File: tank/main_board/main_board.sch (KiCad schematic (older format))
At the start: 38 parts, among them J1 PowerIn, J10 Bump1, J11 Programming Header, J12 SigOut, J13 Encoder0, J14 Encoder1, J16 PowerOut, J2 M1, J20 PowerMotor, J3 M2, J4 LEDs, J5 M0, J6 Spk, J7 Hall2, J8 Hall1, J9 Bump0, Q1 2N3904, U1 L7805, U2 ATMEGA328P-PU, U3 SN74HC595, U4 TB6612FNG, U5 TB6612FNG, Y1 Crystal

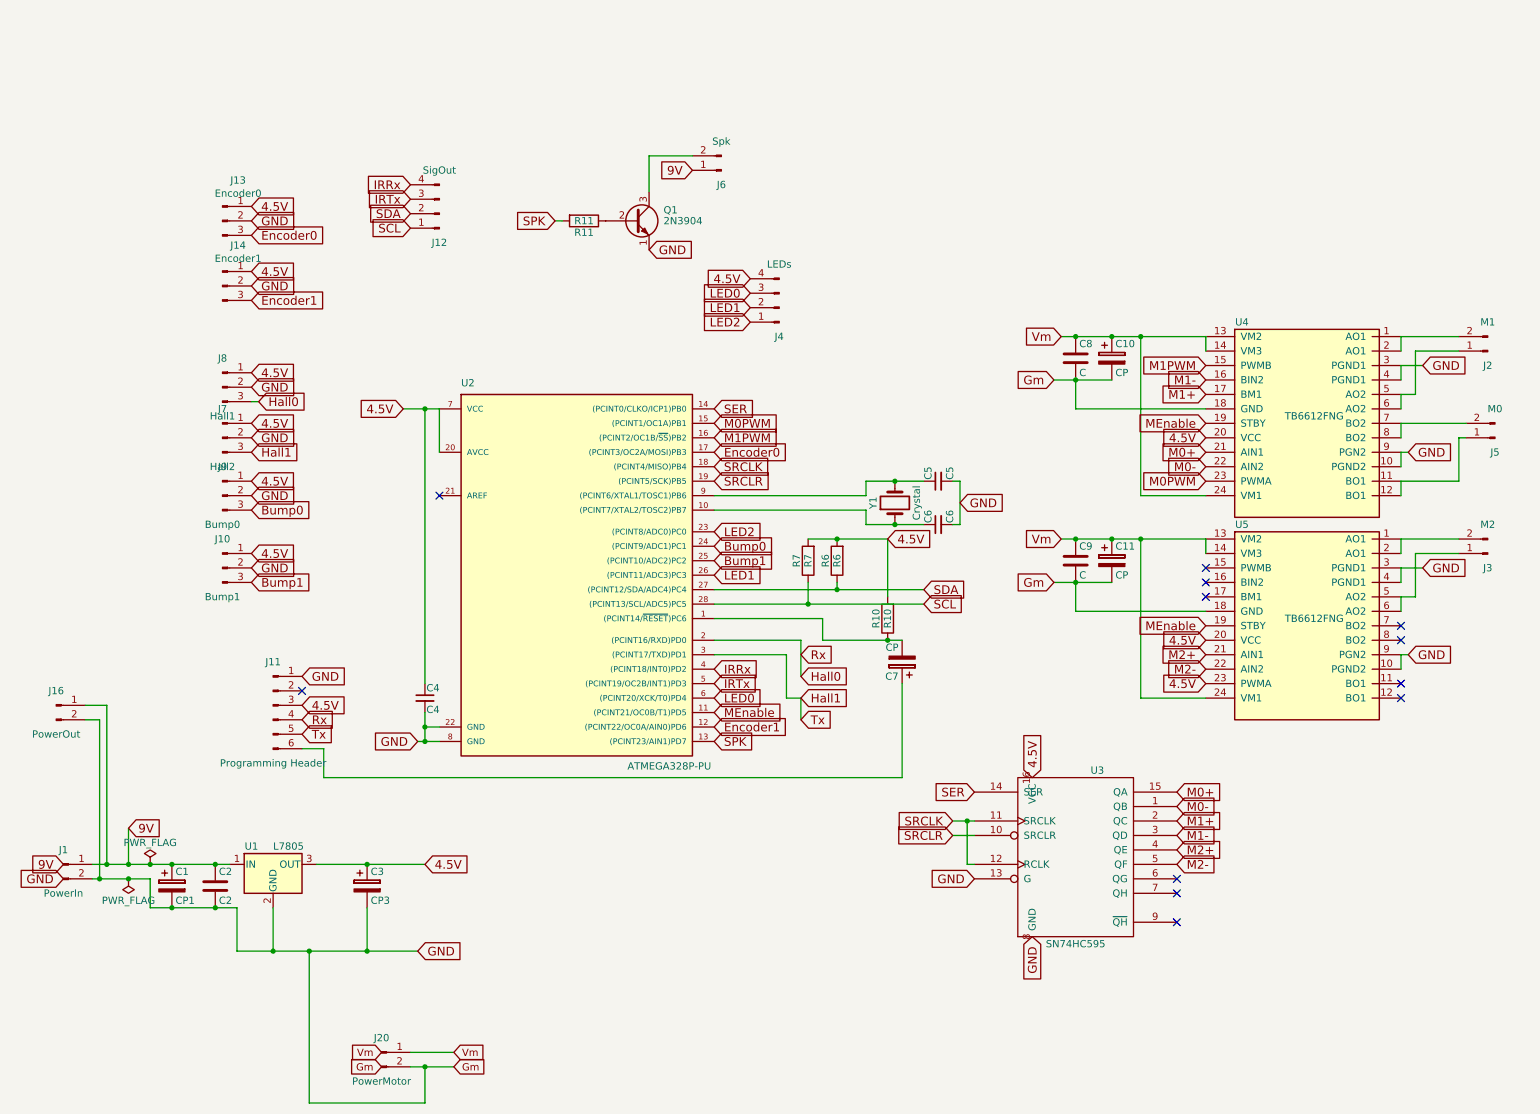
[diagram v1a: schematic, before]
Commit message: Main Board version 0.6: - add ground planes on both layers - LED square is VCC - shorten board slightly - power out is regulated - vias. vias everywhere. - mounting holes embiggened
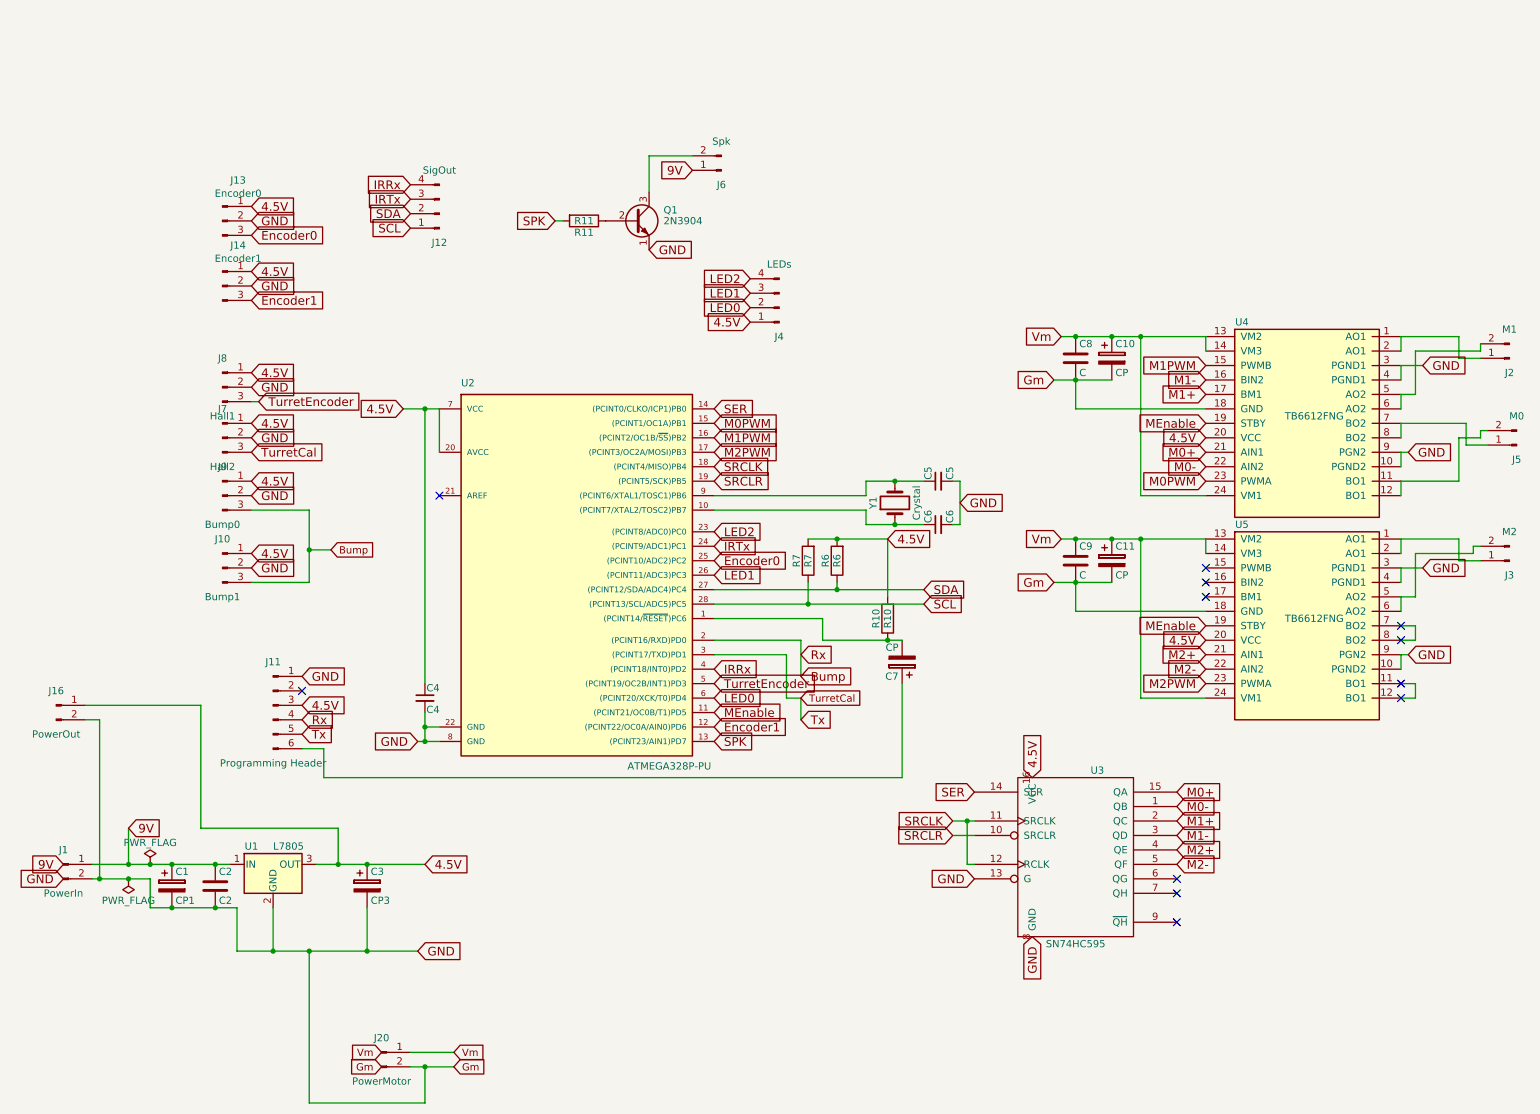
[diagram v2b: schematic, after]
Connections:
- net 4.5V: now also J16.1 (Pin_1), J4.1 (Pin_1); no longer J4.4 (Pin_4), U5.23 (PWMA)
- net 9V: no longer J16.1 (Pin_1)
- net Encoder0: now also U2.25 ((PCINT10/ADC2)PC2); no longer U2.17 ((PCINT3/OC2A/MOSI)PB3)
- net IRTx: now also U2.24 ((PCINT9/ADC1)PC1); no longer U2.5 ((PCINT19/OC2B/INT1)PD3)
- net LED0: now also J4.2 (Pin_2); no longer J4.3 (Pin_3)
- net LED1: now also J4.3 (Pin_3); no longer J4.2 (Pin_2)
- net LED2: now also J4.4 (Pin_4); no longer J4.1 (Pin_1)
- net at U4.1 (AO1), U4.2 (AO1): now also J2.1 (Pin_1); no longer J2.2 (Pin_2)
- net at U4.11 (BO1), U4.12 (BO1): now also J5.2 (Pin_2); no longer J5.1 (Pin_1)
- net at U4.5 (AO2), U4.6 (AO2): now also J2.2 (Pin_2); no longer J2.1 (Pin_1)
- net at U4.7 (BO2), U4.8 (BO2): now also J5.1 (Pin_1); no longer J5.2 (Pin_2)
- net at U5.1 (AO1), U5.2 (AO1): now also J3.1 (Pin_1); no longer J3.2 (Pin_2)
- net at U5.11 (BO1): now also U5.12 (BO1)
- net at U5.5 (AO2), U5.6 (AO2): now also J3.2 (Pin_2); no longer J3.1 (Pin_1)
- net at U5.7 (BO2): now also U5.8 (BO2)
- net Bump0 renamed Bump
- net Bump: now also J10.3 (Pin_3), J11.4 (Pin_4), U2.2 ((PCINT16/RXD)PD0); no longer U2.24 ((PCINT9/ADC1)PC1)
- removed net Bump1: J10.3 (Pin_3), U2.25 ((PCINT10/ADC2)PC2)
- removed net Hall0: J11.4 (Pin_4), J8.3 (Pin_3), U2.2 ((PCINT16/RXD)PD0)
- net Hall1 renamed TurretCal
- new net M2PWM: U2.17 ((PCINT3/OC2A/MOSI)PB3), U5.23 (PWMA)
- new net TurretEncoder: J8.3 (Pin_3), U2.5 ((PCINT19/OC2B/INT1)PD3)
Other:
- moved on the sheet: J2, J3, J5
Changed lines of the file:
@@
-$EndComp
-$Comp
-L main_board-rescue:Conn_01x03_Male J9
-U 1 1 59DE306D
-P 1850 3000
-F 0 "J9" H 1850 3200 50  0000 C CNN
-F 1 "Bump0" H 1850 2800 50  0000 C CNN
-F 2 "JST:JST_EH_B03B-EH-A_03x2.50mm_Straight" H 1850 3000 50  0001 C CNN
-F 3 "" H 1850 3000 50  0001 C CNN
-	1    1850 3000
-	1    0    0    -1
 $EndComp
 $Comp
@@
 $EndComp
 Wire Wire Line
-	950  5550 1050 5550
-Wire Wire Line
 	950  5650 1000 5650
 Wire Wire Line
@@
 Wire Wire Line
 	1200 5550 1200 5300
-Wire Wire Line
-	1050 4450 1050 5550
-Wire Wire Line
-	1050 4450 900  4450
-Connection ~ 1050 5550
 Wire Wire Line
 	900  4550 1000 4550
@@
 Text GLabel 5250 4200 2    60   Input ~ 0
 IRRx
-Text GLabel 5250 4300 2    60   Input ~ 0
+Text GLabel 5250 3350 2    60   Input ~ 0
 IRTx
 Text GLabel 6950 3050 2    60   Input ~ 0
@@
 	10100 2300 10100 2000
 Wire Wire Line
-	10100 2000 10400 2000
-Wire Wire Line
 	10000 2400 10000 2300
 Wire Wire Line
@@
 Wire Wire Line
 	10400 2900 10400 2600
-Wire Wire Line
-	10400 2600 10450 2600
 NoConn ~ 8450 5650
 NoConn ~ 8450 5750
@@
 Text GLabel 7600 2200 0    60   Input ~ 0
 Gm
+Wire Wire Line
+	5250 4000 5850 4000
+Wire Wire Line
+	5850 4000 5850 4250
+Wire Wire Line
+	5250 4100 5750 4100
+Wire Wire Line
+	5750 4100 5750 4400
+Wire Wire Line
+	5750 4400 5850 4400
 Text GLabel 5850 4250 2    60   Input ~ 0
-Hall0
-Text GLabel 5850 4400 2    60   Input ~ 0
-Hall1
-Wire Wire Line
-	5250 4000 5850 4000
-Wire Wire Line
-	5850 4000 5850 4250
-Wire Wire Line
-	5250 4100 5750 4100
-Wire Wire Line
-	5750 4100 5750 4400
-Wire Wire Line
-	5750 4400 5850 4400
-Text GLabel 5250 3450 2    60   Input ~ 0
-Bump1
-Text GLabel 2050 3600 2    60   Input ~ 0
-Bump1
-Text GLabel 5250 3350 2    60   Input ~ 0
-Bump0
-Text GLabel 2050 3100 2    60   Input ~ 0
-Bump0
+Bump
 Text GLabel 2100 2350 2    60   Input ~ 0
-Hall0
+TurretEncoder
 Text GLabel 2050 2700 2    60   Input ~ 0
-Hall1
+TurretCal
+Text GLabel 5500 1800 0    60   Input ~ 0
+4.5V
+Text GLabel 5500 1700 0    60   Input ~ 0
+LED0
+Text GLabel 5500 1600 0    60   Input ~ 0
+LED1
 Text GLabel 5500 1500 0    60   Input ~ 0
-4.5V
-Text GLabel 5500 1600 0    60   Input ~ 0
-LED0
-Text GLabel 5500 1700 0    60   Input ~ 0
-LED1
-Text GLabel 5500 1800 0    60   Input ~ 0
 LED2
 Text GLabel 5250 2500 2    60   Input ~ 0
@@
 Text GLabel 8650 2100 0    60   Input ~ 0
 M1PWM
-Text GLabel 5250 2700 2    60   Input ~ 0
+Text GLabel 5250 3450 2    60   Input ~ 0
 Encoder0
 Text GLabel 5250 2400 2    60   Input ~ 0
@@
 Wire Wire Line
 	10100 3700 10100 3400
-Wire Wire Line
-	10100 3400 10400 3400
 Text GLabel 7650 3300 0    60   Input ~ 0
 Vm
@@
 	6100 3650 6700 3650
 Wire Wire Line
-	1050 5550 1200 5550
-Wire Wire Line
 	6450 4000 6550 4000
 Wire Wire Line
@@
 	6950 2900 6950 3200
 Wire Wire Line
-	2500 5550 2850 5550
+	2500 5550 2650 5550
 Wire Wire Line
 	1000 5650 1200 5650
@@
 Wire Wire Line
 	7750 3800 7750 3600
-Text GLabel 8650 4300 0    60   Input ~ 0
-4.5V
 $Comp
 L main_board-rescue:Conn_01x03_Male J13
@@
 L main_board-rescue:Conn_01x02_Male J2
 U 1 1 5E9835C0
-P 10600 2000
-F 0 "J2" H 10600 2100 50  0000 C CNN
-F 1 "M1" H 10600 1800 50  0000 C CNN
-F 2 "JST:JST_EH_B02B-EH-A_02x2.50mm_Straight" H 10600 2000 50  0001 C CNN
-F 3 "" H 10600 2000 50  0001 C CNN
-	1    10600 2000
+P 10750 2050
+F 0 "J2" H 10750 2150 50  0000 C CNN
+F 1 "M1" H 10750 1850 50  0000 C CNN
+F 2 "JST:JST_EH_B02B-EH-A_02x2.50mm_Straight" H 10750 2050 50  0001 C CNN
+F 3 "" H 10750 2050 50  0001 C CNN
+	1    10750 2050
 	-1   0    0    1
 $EndComp
@@
 L main_board-rescue:Conn_01x02_Male J5
 U 1 1 5E98A5F8
-P 10650 2600
-F 0 "J5" H 10650 2700 50  0000 C CNN
-F 1 "M0" H 10650 2400 50  0000 C CNN
-F 2 "JST:JST_EH_B02B-EH-A_02x2.50mm_Straight" H 10650 2600 50  0001 C CNN
-F 3 "" H 10650 2600 50  0001 C CNN
-	1    10650 2600
+P 10800 2650
+F 0 "J5" H 10800 2750 50  0000 C CNN
+F 1 "M0" H 10800 2450 50  0000 C CNN
+F 2 "JST:JST_EH_B02B-EH-A_02x2.50mm_Straight" H 10800 2650 50  0001 C CNN
+F 3 "" H 10800 2650 50  0001 C CNN
+	1    10800 2650
 	-1   0    0    1
 $EndComp
+Text GLabel 5250 2700 2    60   Input ~ 0
+M2PWM
+Text GLabel 8650 4300 0    60   Input ~ 0
+M2PWM
+Text GLabel 5250 4300 2    60   Input ~ 0
+TurretEncoder
+$Comp
+L main_board-rescue:Conn_01x03_Male J9
+U 1 1 59DE306D
+P 1850 3000
+F 0 "J9" H 1850 3200 50  0000 C CNN
+F 1 "Bump0" H 1850 2800 50  0000 C CNN
+F 2 "JST:JST_EH_B03B-EH-A_03x2.50mm_Straight" H 1850 3000 50  0001 C CNN
+F 3 "" H 1850 3000 50  0001 C CNN
+	1    1850 3000
+	1    0    0    -1
+$EndComp
+Wire Wire Line
+	2050 3100 2450 3100
+Wire Wire Line
+	2450 3100 2450 3375
+Wire Wire Line
+	2450 3375 2600 3375
+Wire Wire Line
+	2450 3600 2450 3375
+Connection ~ 2450 3375
+Text GLabel 2600 3375 2    50   Input ~ 0
+Bump
+Wire Wire Line
+	2450 3600 2050 3600
+Text GLabel 5850 4400 2    50   Input ~ 0
+TurretCal
 $Comp
 L main_board-rescue:Conn_01x02_Male J3
 U 1 1 5E98F9A1
-P 10600 3400
-F 0 "J3" H 10600 3500 50  0000 C CNN
-F 1 "M2" H 10600 3200 50  0000 C CNN
-F 2 "JST:JST_EH_B02B-EH-A_02x2.50mm_Straight" H 10600 3400 50  0001 C CNN
-F 3 "" H 10600 3400 50  0001 C CNN
-	1    10600 3400
+P 10750 3450
+F 0 "J3" H 10750 3550 50  0000 C CNN
+F 1 "M2" H 10750 3250 50  0000 C CNN
+F 2 "JST:JST_EH_B02B-EH-A_02x2.50mm_Straight" H 10750 3450 50  0001 C CNN
+F 3 "" H 10750 3450 50  0001 C CNN
+	1    10750 3450
 	-1   0    0    1
 $EndComp
+Wire Wire Line
+	10550 2000 10550 1950
+Wire Wire Line
+	10100 2000 10550 2000
+Wire Wire Line
+	10400 1900 10400 2050
+Wire Wire Line
+	10400 2050 10550 2050
+Wire Wire Line
+	10550 2600 10550 2550
+Wire Wire Line
+	10550 2550 10600 2550
+Wire Wire Line
+	10400 2600 10550 2600
+Wire Wire Line
+	10450 2500 10450 2650
+Wire Wire Line
+	10450 2650 10600 2650
+Wire Wire Line
+	10500 3400 10500 3350
+Wire Wire Line
+	10500 3350 10550 3350
+Wire Wire Line
+	10100 3400 10500 3400
+Wire Wire Line
+	10400 3300 10400 3450
+Wire Wire Line
+	10400 3450 10550 3450
+Wire Wire Line
+	10000 4000 10100 4000
+Wire Wire Line
+	10100 4000 10100 3900
+Wire Wire Line
+	10100 3900 10000 3900
+Wire Wire Line
+	10000 4300 10100 4300
+Wire Wire Line
+	10100 4300 10100 4400
+Wire Wire Line
+	10100 4400 10000 4400
+Wire Wire Line
+	950  5550 1200 5550
+Wire Wire Line
+	1700 4450 1700 5300
+Wire Wire Line
+	1700 5300 2650 5300
+Wire Wire Line
+	2650 5300 2650 5550
+Wire Wire Line
+	900  4450 1700 4450
+Connection ~ 2650 5550
+Wire Wire Line
+	2650 5550 2850 5550
 $EndSCHEMATC

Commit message: Main Board Version 0.7
Had to switch around pins. Need M0 and M1 on the same PWM timer.
Need IR receiver pin to not interfere.
No point in ground traces with a ground plane.
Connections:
- net Encoder1: now also U2.17 ((PCINT3/OC2A/MOSI)PB3); no longer U2.12 ((PCINT22/OC0A/AIN0)PD6)
- net IRRx: now also U2.5 ((PCINT19/OC2B/INT1)PD3); no longer U2.4 ((PCINT18/INT0)PD2)
- net M0PWM: now also U2.11 ((PCINT21/OC0B/T1)PD5); no longer U2.15 ((PCINT1/OC1A)PB1)
- net M1PWM: now also U2.12 ((PCINT22/OC0A/AIN0)PD6); no longer U2.16 ((PCINT2/OC1B/~SS~)PB2)
- net M2PWM: now also U2.15 ((PCINT1/OC1A)PB1); no longer U2.17 ((PCINT3/OC2A/MOSI)PB3)
- net MEnable: now also U2.16 ((PCINT2/OC1B/~SS~)PB2); no longer U2.11 ((PCINT21/OC0B/T1)PD5)
- net TurretEncoder: now also U2.4 ((PCINT18/INT0)PD2); no longer U2.5 ((PCINT19/OC2B/INT1)PD3)
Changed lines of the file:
@@
 Text GLabel 2050 3500 2    60   Input ~ 0
 GND
-Text GLabel 5250 4500 2    60   Input ~ 0
+Text GLabel 5250 2600 2    60   Input ~ 0
 MEnable
 Text GLabel 5250 4400 2    60   Input ~ 0
@@
 Text GLabel 3100 2400 0    60   Input ~ 0
 4.5V
-Text GLabel 5250 4200 2    60   Input ~ 0
+Text GLabel 5250 4300 2    60   Input ~ 0
 IRRx
 Text GLabel 5250 3350 2    60   Input ~ 0
@@
 Text GLabel 5500 1500 0    60   Input ~ 0
 LED2
-Text GLabel 5250 2500 2    60   Input ~ 0
+Text GLabel 5250 4500 2    60   Input ~ 0
 M0PWM
 Text GLabel 8650 2900 0    60   Input ~ 0
 M0PWM
-Text GLabel 5250 2600 2    60   Input ~ 0
+Text GLabel 5250 4600 2    60   Input ~ 0
 M1PWM
 Text GLabel 8650 2100 0    60   Input ~ 0
@@
 Text GLabel 5250 3250 2    60   Input ~ 0
 LED2
-Text GLabel 5250 4600 2    60   Input ~ 0
+Text GLabel 5250 2700 2    60   Input ~ 0
 Encoder1
 Text GLabel 8450 5450 2    60   Input ~ 0
@@
 	-1   0    0    1
 $EndComp
-Text GLabel 5250 2700 2    60   Input ~ 0
+Text GLabel 5250 2500 2    60   Input ~ 0
 M2PWM
 Text GLabel 8650 4300 0    60   Input ~ 0
 M2PWM
-Text GLabel 5250 4300 2    60   Input ~ 0
+Text GLabel 5250 4200 2    60   Input ~ 0
 TurretEncoder
 $Comp

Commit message: main board updates
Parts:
- removed C7: CP, Capacitors_THT:CP_Radial_D4.0mm_P2.00mm, symbol main_board-rescue:CP
- added C7: C_Small, symbol Device:C_Small
- J10: symbol main_board-rescue:Conn_01x03_Male -> main_board-rescue:Conn_01x02_Male
- J7: value Hall2 -> Encoder3
- J8: value Hall1 -> Encoder2
- J9: footprint JST:JST_EH_B03B-EH-A_03x2.50mm_Straight -> Connector_JST:JST_EH_B2B-EH-A_1x02_P2.50mm_Vertical; symbol main_board-rescue:Conn_01x03_Male -> main_board-rescue:Conn_01x02_Male
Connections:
- net 4.5V: no longer J10.1 (Pin_1), J9.1 (Pin_1)
- net Bump: now also J10.2 (Pin_2), J9.2 (Pin_2); no longer J10.3 (Pin_3), J9.3 (Pin_3)
- net GND: now also J10.1 (Pin_1), J9.1 (Pin_1); no longer J10.2 (Pin_2), J9.2 (Pin_2)
- net at R10.1, U2.1 ((PCINT14/~RESET~)PC6): now also C7.1
- net at J11.6 (Pin_6): now also C7.2
- net TurretCal renamed Encoder3
- net TurretEncoder renamed Encoder2
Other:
- moved on the sheet: J7, J8
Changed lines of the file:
@@
 L main_board-rescue:Conn_01x03_Male J8
 U 1 1 59DDB019
+P 1850 1900
+F 0 "J8" H 1850 2100 50  0000 C CNN
+F 1 "Encoder2" H 1850 1700 50  0000 C CNN
+F 2 "JST:JST_EH_B03B-EH-A_03x2.50mm_Straight" H 1850 1900 50  0001 C CNN
+F 3 "" H 1850 1900 50  0001 C CNN
+	1    1850 1900
+	1    0    0    -1
+$EndComp
+$Comp
+L main_board-rescue:Conn_01x03_Male J7
+U 1 1 59DDB307
 P 1850 2250
-F 0 "J8" H 1850 2450 50  0000 C CNN
-F 1 "Hall1" H 1850 2050 50  0000 C CNN
+F 0 "J7" H 1850 2450 50  0000 C CNN
+F 1 "Encoder3" H 1850 2050 50  0000 C CNN
 F 2 "JST:JST_EH_B03B-EH-A_03x2.50mm_Straight" H 1850 2250 50  0001 C CNN
 F 3 "" H 1850 2250 50  0001 C CNN
 	1    1850 2250
-	1    0    0    -1
-$EndComp
-$Comp
-L main_board-rescue:Conn_01x03_Male J7
-U 1 1 59DDB307
-P 1850 2600
-F 0 "J7" H 1850 2800 50  0000 C CNN
-F 1 "Hall2" H 1850 2400 50  0000 C CNN
-F 2 "JST:JST_EH_B03B-EH-A_03x2.50mm_Straight" H 1850 2600 50  0001 C CNN
-F 3 "" H 1850 2600 50  0001 C CNN
-	1    1850 2600
 	1    0    0    -1
 $EndComp
@@
 $EndComp
 $Comp
-L main_board-rescue:Conn_01x03_Male J10
+L main_board-rescue:Conn_01x02_Male J10
 U 1 1 59DE3178
 P 1850 3500
@@
 	-1   0    0    1
 $EndComp
-$Comp
-L main_board-rescue:CP C7
-U 1 1 59FE341B
-P 6550 4150
-F 0 "C7" H 6575 4250 50  0000 L CNN
-F 1 "CP" H 6575 4050 50  0000 L CNN
-F 2 "Capacitors_THT:CP_Radial_D4.0mm_P2.00mm" H 6588 4000 50  0001 C CNN
-F 3 "" H 6550 4150 50  0001 C CNN
-	1    6550 4150
-	-1   0    0    1
-$EndComp
 NoConn ~ 2400 4350
 $Comp
@@
 	2550 4950 6550 4950
 Wire Wire Line
-	6550 4950 6550 4300
-Wire Wire Line
 	3250 4500 3250 4600
 Wire Wire Line
-	2100 2350 2050 2350
+	2100 2000 2050 2000
 Wire Wire Line
 	4150 1100 4200 1100
@@
 Text GLabel 2400 4650 2    60   Input ~ 0
 Tx
-Text GLabel 2050 2500 2    60   Input ~ 0
-4.5V
-Text GLabel 2050 2600 2    60   Input ~ 0
-GND
 Text GLabel 2050 2150 2    60   Input ~ 0
 4.5V
-Text GLabel 2050 2900 2    60   Input ~ 0
-4.5V
-Text GLabel 2050 3400 2    60   Input ~ 0
-4.5V
 Text GLabel 2050 2250 2    60   Input ~ 0
+GND
+Text GLabel 2050 1800 2    60   Input ~ 0
+4.5V
+Text GLabel 2050 1900 2    60   Input ~ 0
 GND
 Text GLabel 2050 3000 2    60   Input ~ 0
@@
 Text GLabel 5850 4250 2    60   Input ~ 0
 Bump
-Text GLabel 2100 2350 2    60   Input ~ 0
-TurretEncoder
-Text GLabel 2050 2700 2    60   Input ~ 0
-TurretCal
+Text GLabel 2100 2000 2    60   Input ~ 0
+Encoder2
+Text GLabel 2050 2350 2    60   Input ~ 0
+Encoder3
 Text GLabel 5500 1800 0    60   Input ~ 0
 4.5V
@@
 M2PWM
 Text GLabel 5250 4200 2    60   Input ~ 0
-TurretEncoder
-$Comp
-L main_board-rescue:Conn_01x03_Male J9
+Encoder2
+$Comp
+L main_board-rescue:Conn_01x02_Male J9
 U 1 1 59DE306D
 P 1850 3000
 F 0 "J9" H 1850 3200 50  0000 C CNN
 F 1 "Bump0" H 1850 2800 50  0000 C CNN
-F 2 "JST:JST_EH_B03B-EH-A_03x2.50mm_Straight" H 1850 3000 50  0001 C CNN
+F 2 "Connector_JST:JST_EH_B2B-EH-A_1x02_P2.50mm_Vertical" H 1850 3000 50  0001 C CNN
 F 3 "" H 1850 3000 50  0001 C CNN
 	1    1850 3000
@@
 	2450 3600 2050 3600
 Text GLabel 5850 4400 2    50   Input ~ 0
-TurretCal
+Encoder3
 $Comp
 L main_board-rescue:Conn_01x02_Male J3
@@
 Wire Wire Line
 	2650 5550 2850 5550
+$Comp
+L Device:C_Small C7
+U 1 1 61727AF7
+P 6550 4100
+F 0 "C7" H 6642 4146 50  0000 L CNN
+F 1 "C_Small" H 6642 4055 50  0000 L CNN
+F 2 "" H 6550 4100 50  0001 C CNN
+F 3 "~" H 6550 4100 50  0001 C CNN
+	1    6550 4100
+	1    0    0    -1
+$EndComp
+Wire Wire Line
+	6550 4200 6550 4950
 $EndSCHEMATC
